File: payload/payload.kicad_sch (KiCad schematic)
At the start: 11 parts, among them J101 Conn_02x26_Odd_Even, J102 Conn_02x26_Odd_Even, U101 PCA9548APW

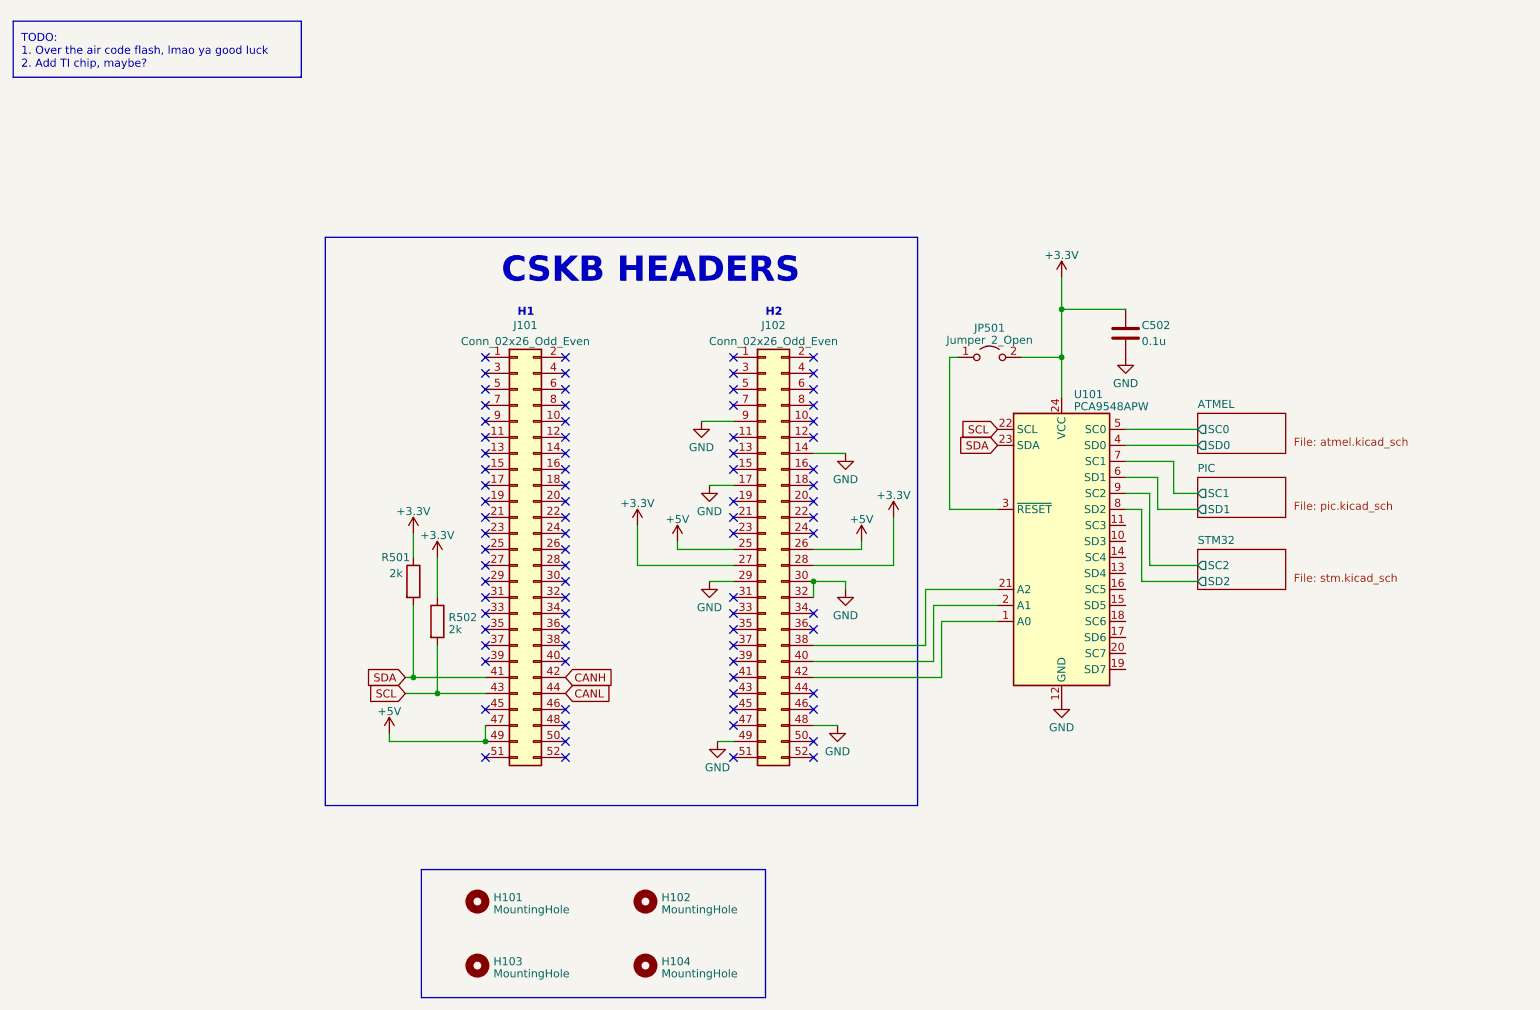
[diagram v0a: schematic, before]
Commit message: added TPs
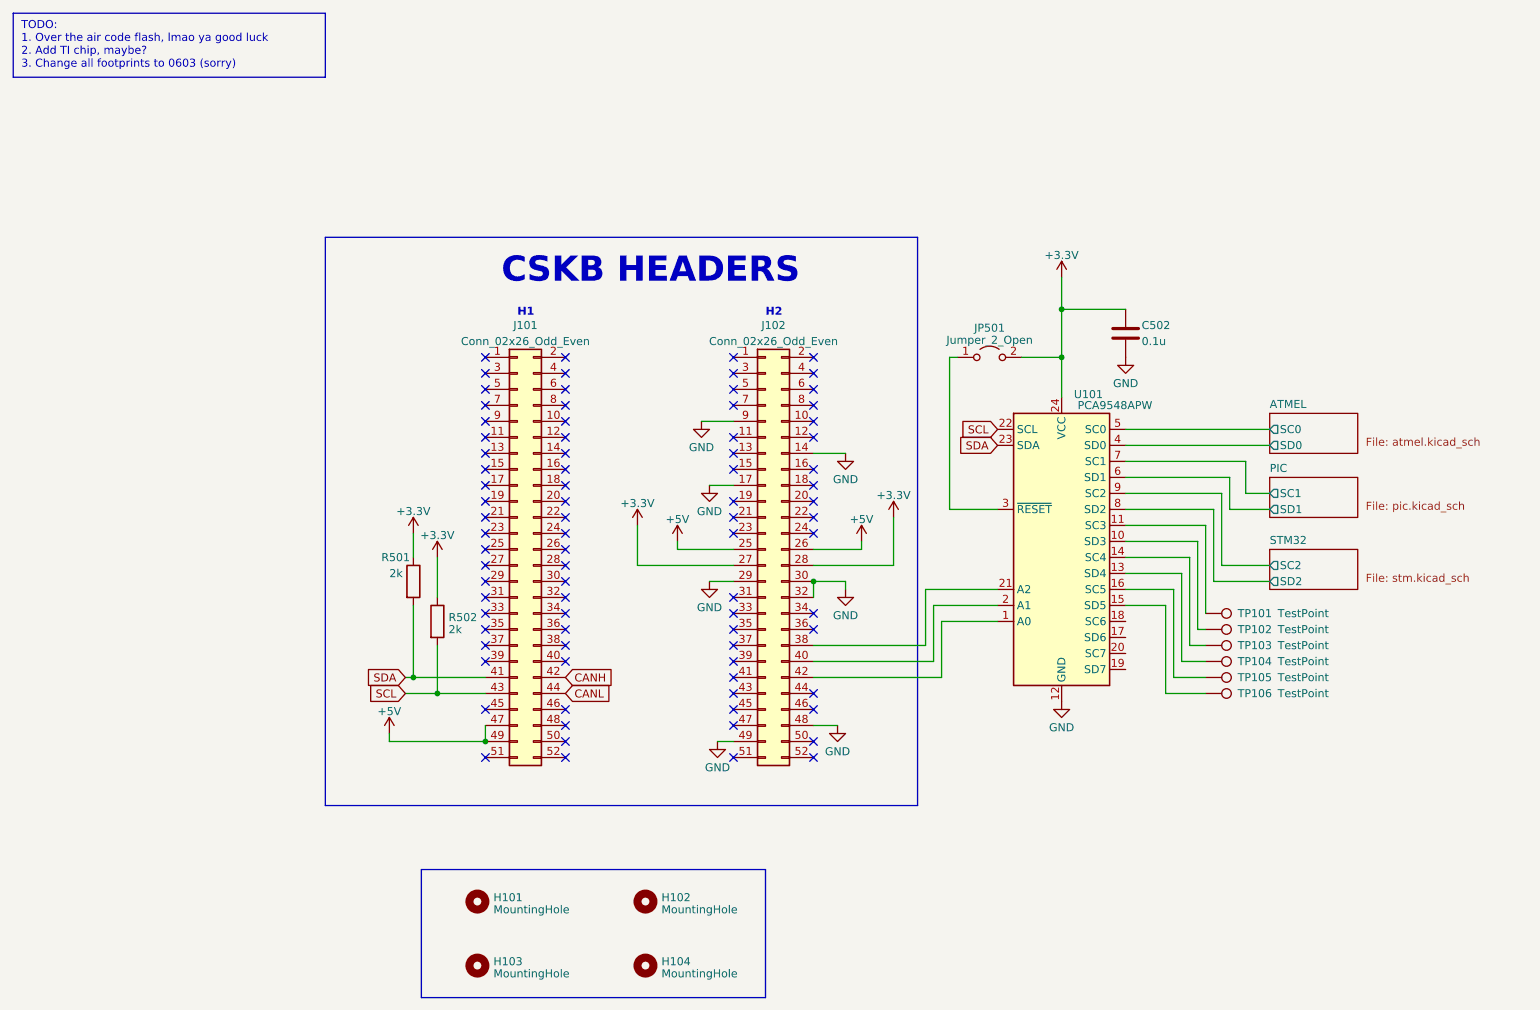
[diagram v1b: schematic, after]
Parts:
- added TP101, TP102, TP103, TP104, TP105, TP106: TestPoint, TestPoint:TestPoint_THTPad_1.0x1.0mm_Drill0.5mm, symbol Connector:TestPoint
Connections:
- net at U101.10 (SD3): now also TP102.1
- net at U101.11 (SC3): now also TP101.1
- net at U101.13 (SD4): now also TP104.1
- net at U101.14 (SC4): now also TP103.1
- net at U101.15 (SD5): now also TP106.1
- net at U101.16 (SC5): now also TP105.1
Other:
- note added: "TODO: 1. Over the air code flash, lmao ya good luck 2. Add TI chip, maybe? 3. Change all footprints to 0603 (sorry)"
- note removed: "TODO: 1. Over the air code flash, lmao ya good luck 2. Add TI chip, maybe?"
